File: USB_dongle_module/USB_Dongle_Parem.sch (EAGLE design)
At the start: 25 parts, among them IC3 FT230XS, X1 USB-A, X2 MICROMATCH-6

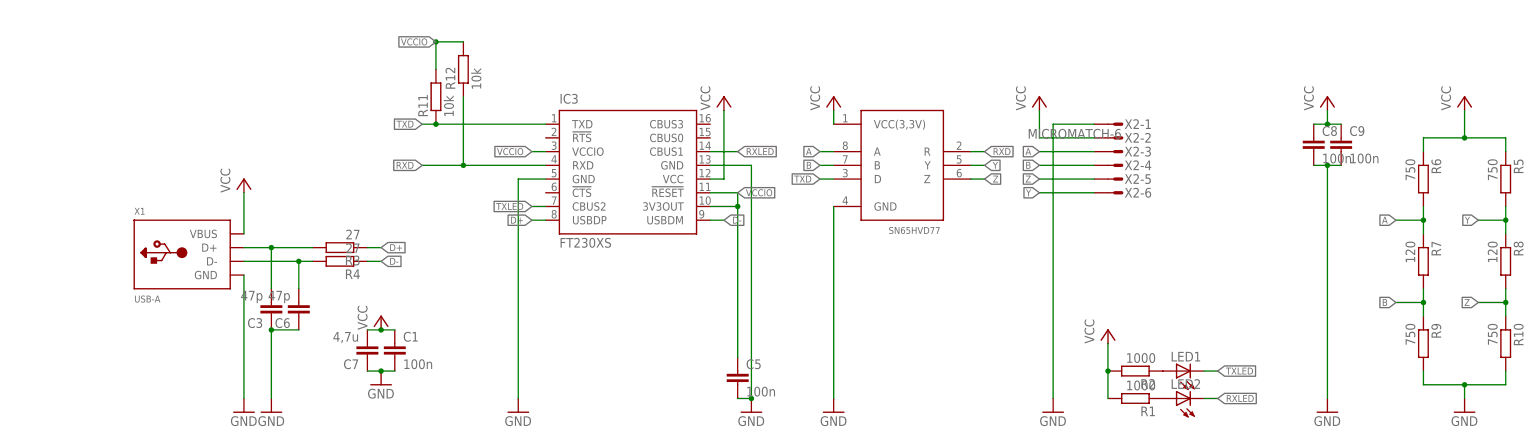
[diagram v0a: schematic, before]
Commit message: Rerouted USB dongle
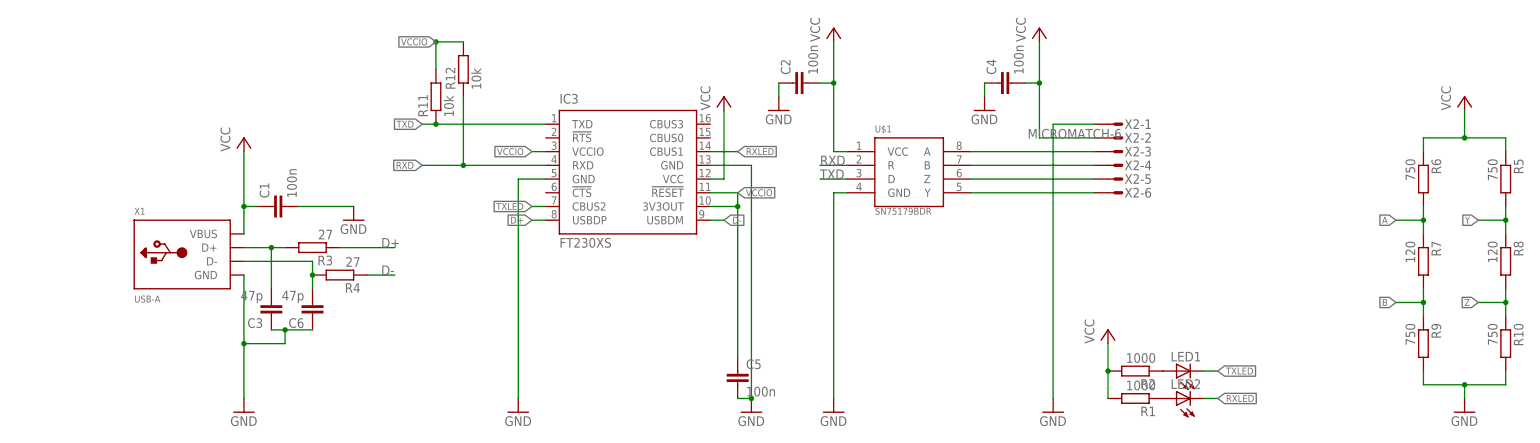
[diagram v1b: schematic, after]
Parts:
- removed C7: 4,7u, eagle-ltspice:CC1206
- removed C8, C9: 100n, eagle-ltspice:CC0603
- removed U$2: SN65HVD77D, Kommunikatsioon:SN65HVD77D
- added C2, C4: 100n, eagle-ltspice:CC0603
- added U$1: SN75179BDR, SparkFun-DigitalIC:SN75179BDR
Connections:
- net A: now also U$1.A; no longer U$2.A
- net B: now also U$1.B; no longer U$2.B
- net GND: now also C2.1, C4.1, U$1.GND; no longer C7.1, C8.2, C9.2, U$2.GND
- net RXD: now also U$1.R; no longer U$2.R
- net TXD: now also U$1.D; no longer U$2.D
- net VCC: now also C2.2, C4.2, U$1.VCC; no longer C7.2, C8.1, C9.1, U$2.VCC(3,3V)
- net Y: now also U$1.Y; no longer U$2.Y
- net Z: now also U$1.Z; no longer U$2.Z
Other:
- moved on the sheet: C1, C6, R3, R4

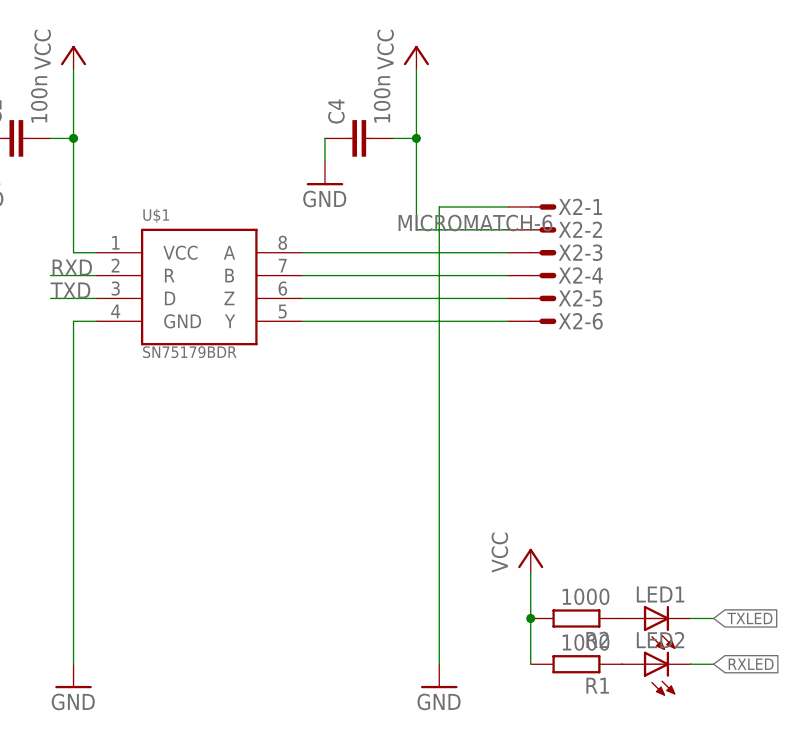
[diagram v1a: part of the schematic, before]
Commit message: Fixed AB-YZ GND-VCC bugs
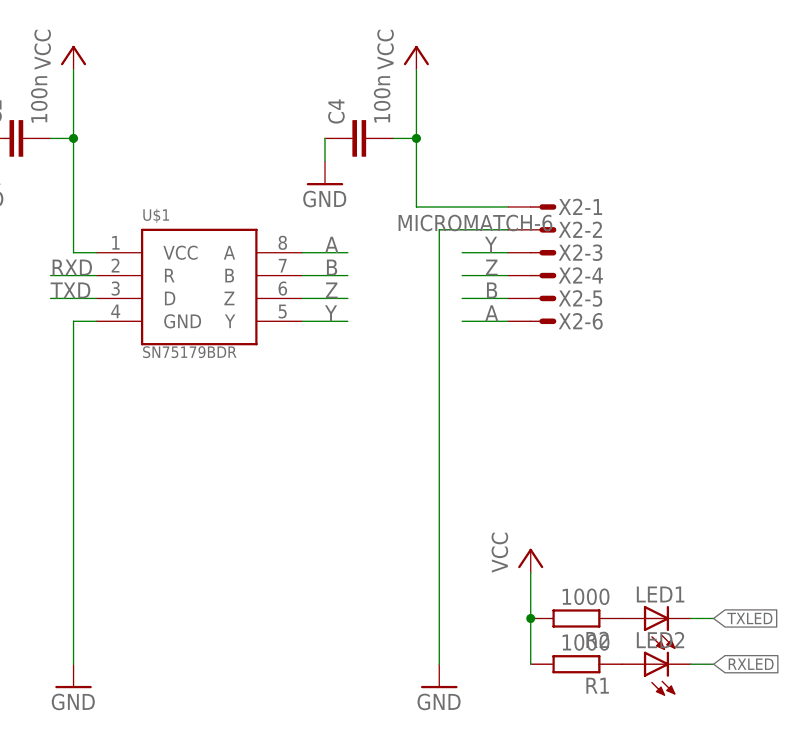
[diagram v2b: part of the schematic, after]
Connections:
- net A: now also X2-6.S; no longer X2-3.S
- net B: now also X2-5.S; no longer X2-4.S
- net GND: now also X2-2.S; no longer X2-1.S
- net VCC: now also X2-1.S; no longer X2-2.S
- net Y: now also X2-3.S; no longer X2-6.S
- net Z: now also X2-4.S; no longer X2-5.S
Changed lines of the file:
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@@
-</segment>
-<segment>
-<wire x1="165.1" y1="106.68" x2="172.72" y2="106.68" width="0.1524" layer="91"/>
-<wire x1="165.1" y1="106.68" x2="165.1" y2="55.88" width="0.1524" layer="91"/>
-<pinref part="GND6" gate="1" pin="GND"/>
-<pinref part="X2" gate="-1" pin="S"/>
 </segment>
 <segment>
@@
 <wire x1="152.4" y1="111.76" x2="152.4" y2="114.3" width="0.1524" layer="91"/>
 </segment>
+<segment>
+<pinref part="X2" gate="-2" pin="S"/>
+<pinref part="GND6" gate="1" pin="GND"/>
+<wire x1="172.72" y1="104.14" x2="165.1" y2="104.14" width="0.1524" layer="91"/>
+<wire x1="165.1" y1="104.14" x2="165.1" y2="55.88" width="0.1524" layer="91"/>
+</segment>
 </net>
 <net name="VCC" class="0">
@@
 </segment>
 <segment>
-<wire x1="172.72" y1="104.14" x2="162.56" y2="104.14" width="0.1524" layer="91"/>
-<wire x1="162.56" y1="104.14" x2="162.56" y2="114.3" width="0.1524" layer="91"/>
+<wire x1="162.56" y1="106.68" x2="162.56" y2="114.3" width="0.1524" layer="91"/>
 <pinref part="P+8" gate="VCC" pin="VCC"/>
-<pinref part="X2" gate="-2" pin="S"/>
 <pinref part="C4" gate="G$1" pin="2"/>
 <wire x1="162.56" y1="114.3" x2="162.56" y2="121.92" width="0.1524" layer="91"/>
 <wire x1="162.56" y1="114.3" x2="160.02" y2="114.3" width="0.1524" layer="91"/>
 <junction x="162.56" y="114.3"/>
+<pinref part="X2" gate="-1" pin="S"/>
+<wire x1="172.72" y1="106.68" x2="162.56" y2="106.68" width="0.1524" layer="91"/>
 </segment>
 <segment>
@@
 </segment>
 <segment>
-<pinref part="X2" gate="-4" pin="S"/>
 <pinref part="U$1" gate="G$1" pin="B"/>
-<wire x1="172.72" y1="99.06" x2="149.86" y2="99.06" width="0.1524" layer="91"/>
+<wire x1="149.86" y1="99.06" x2="154.94" y2="99.06" width="0.1524" layer="91"/>
+<label x="152.4" y="99.06" size="1.778" layer="95"/>
+</segment>
+<segment>
+<pinref part="X2" gate="-5" pin="S"/>
+<wire x1="172.72" y1="96.52" x2="167.64" y2="96.52" width="0.1524" layer="91"/>
+<label x="170.18" y="96.52" size="1.778" layer="95"/>
 </segment>
 </net>
@@
 </segment>
 <segment>
-<pinref part="X2" gate="-6" pin="S"/>
+<pinref part="X2" gate="-3" pin="S"/>
+<wire x1="172.72" y1="101.6" x2="167.64" y2="101.6" width="0.1524" layer="91"/>
+<label x="170.18" y="101.6" size="1.778" layer="95"/>
+</segment>
+<segment>
 <pinref part="U$1" gate="G$1" pin="Y"/>
-<wire x1="172.72" y1="93.98" x2="149.86" y2="93.98" width="0.1524" layer="91"/>
+<wire x1="149.86" y1="93.98" x2="154.94" y2="93.98" width="0.1524" layer="91"/>
+<label x="152.4" y="93.98" size="1.778" layer="95"/>
 </segment>
 </net>
@@
 </segment>
 <segment>
+<pinref part="X2" gate="-4" pin="S"/>
+<wire x1="172.72" y1="99.06" x2="167.64" y2="99.06" width="0.1524" layer="91"/>
+<label x="170.18" y="99.06" size="1.778" layer="95"/>
+</segment>
+<segment>
 <pinref part="U$1" gate="G$1" pin="Z"/>
-<pinref part="X2" gate="-5" pin="S"/>
-<wire x1="149.86" y1="96.52" x2="172.72" y2="96.52" width="0.1524" layer="91"/>
+<wire x1="149.86" y1="96.52" x2="154.94" y2="96.52" width="0.1524" layer="91"/>
+<label x="152.4" y="96.52" size="1.778" layer="95"/>
 </segment>
 </net>
@@
 <segment>
 <pinref part="U$1" gate="G$1" pin="A"/>
-<pinref part="X2" gate="-3" pin="S"/>
-<wire x1="149.86" y1="101.6" x2="172.72" y2="101.6" width="0.1524" layer="91"/>
-</segment>
-</net>
+<wire x1="149.86" y1="101.6" x2="154.94" y2="101.6" width="0.1524" layer="91"/>
+<label x="152.4" y="101.6" size="1.778" layer="95"/>
+</segment>
+<segment>
+<pinref part="X2" gate="-6" pin="S"/>
+<wire x1="172.72" y1="93.98" x2="167.64" y2="93.98" width="0.1524" layer="91"/>
+<label x="170.18" y="93.98" size="1.778" layer="95"/>
+</segment>
+</net>

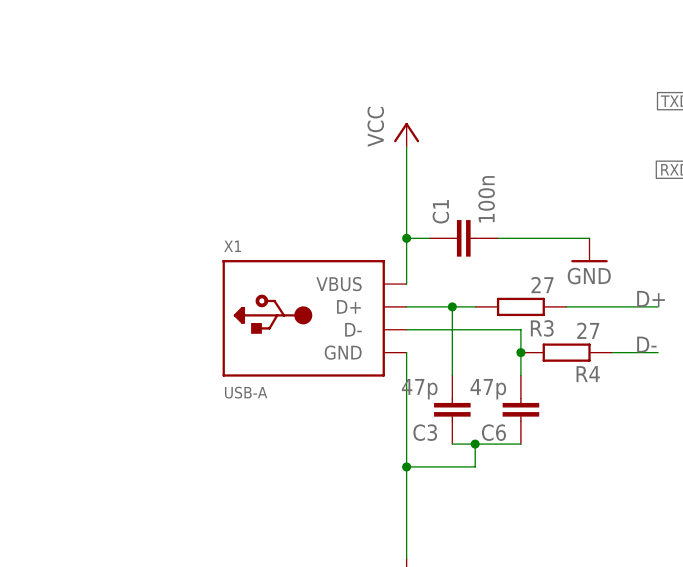
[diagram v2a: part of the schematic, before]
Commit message: USB D+/D- fixes
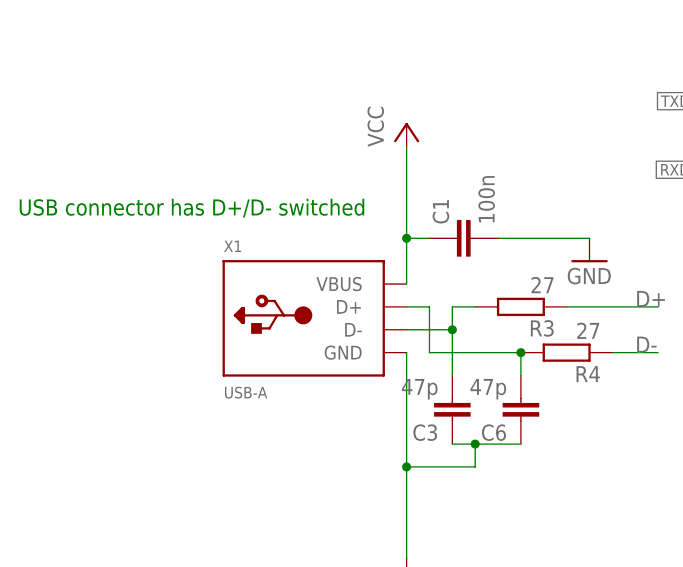
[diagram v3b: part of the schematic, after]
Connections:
- net SA: now also X1.D-; no longer X1.D+
- net SAD: now also X1.D+; no longer X1.D-
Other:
- note added: "USB connector has D+/D- switched"
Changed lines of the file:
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@@
 <sheet>
 <plain>
+<text x="-27.94" y="93.98" size="1.778" layer="91">USB connector has D+/D- switched</text>
 </plain>
 <instances>
@@
 <net name="SA" class="0">
 <segment>
-<pinref part="X1" gate="G$1" pin="D+"/>
 <wire x1="22.86" y1="83.82" x2="20.32" y2="83.82" width="0.1524" layer="91"/>
 <pinref part="R3" gate="G$1" pin="2"/>
 <pinref part="C3" gate="G$1" pin="2"/>
-<wire x1="20.32" y1="83.82" x2="15.24" y2="83.82" width="0.1524" layer="91"/>
-<wire x1="20.32" y1="83.82" x2="20.32" y2="76.2" width="0.1524" layer="91"/>
-<junction x="20.32" y="83.82"/>
+<wire x1="20.32" y1="83.82" x2="20.32" y2="81.28" width="0.1524" layer="91"/>
+<pinref part="X1" gate="G$1" pin="D-"/>
+<wire x1="20.32" y1="81.28" x2="20.32" y2="76.2" width="0.1524" layer="91"/>
+<wire x1="15.24" y1="81.28" x2="20.32" y2="81.28" width="0.1524" layer="91"/>
+<junction x="20.32" y="81.28"/>
 </segment>
 </net>
@@
 <pinref part="C6" gate="G$1" pin="2"/>
 <wire x1="27.94" y1="76.2" x2="27.94" y2="78.74" width="0.1524" layer="91"/>
-<wire x1="27.94" y1="78.74" x2="27.94" y2="81.28" width="0.1524" layer="91"/>
+<pinref part="X1" gate="G$1" pin="D+"/>
+<wire x1="15.24" y1="83.82" x2="17.78" y2="83.82" width="0.1524" layer="91"/>
+<wire x1="17.78" y1="83.82" x2="17.78" y2="78.74" width="0.1524" layer="91"/>
+<wire x1="17.78" y1="78.74" x2="27.94" y2="78.74" width="0.1524" layer="91"/>
 <junction x="27.94" y="78.74"/>
-<pinref part="X1" gate="G$1" pin="D-"/>
-<wire x1="27.94" y1="81.28" x2="15.24" y2="81.28" width="0.1524" layer="91"/>
-</segment>
-</net>
+</segment>
+</net>
